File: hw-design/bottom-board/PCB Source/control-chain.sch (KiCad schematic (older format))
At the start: 20 parts, among them J15 RJHSE-5381, Q5 BSS84, Q6 BSS84, U18 ISL83086E

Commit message: change CC connector
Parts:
- removed C67, C68: 10uF, Capacitor_SMD:C_0603_1608Metric, symbol bottom-board-rescue:C_Small-Device
- removed J15: RJHSE-5381, Connector_RJ:RJ45_Amphenol_RJHSE538X, symbol bottom-board-rescue:RJ45_LED_Shielded-Connector
- removed Q5, Q6: BSS84, Package_TO_SOT_SMD:SOT-23, symbol bottom-board-rescue:BSS84-Transistor_FET
- removed R41, R42: 220R, Resistor_SMD:R_0603_1608Metric, symbol bottom-board-rescue:R_Small-Device
- added J?: RJ45, digikey-footprints:Ethernet_Jack_54602-908LF, symbol Connector:RJ45
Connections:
- net labels removed: RS485_RX_LED, RS485_TX_LED
- wire segments 87 -> 60

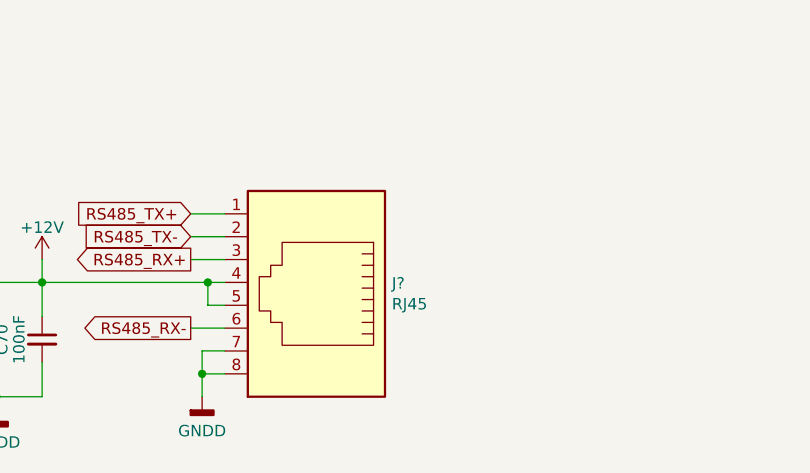
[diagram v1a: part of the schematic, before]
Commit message: place new power curcuit on the PCB
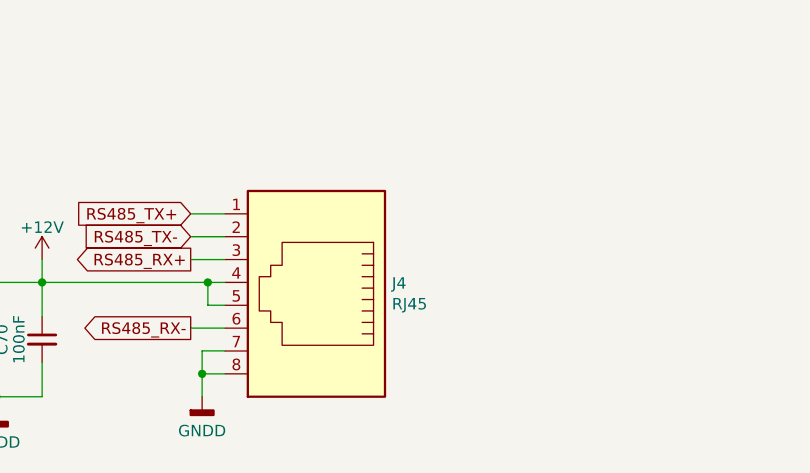
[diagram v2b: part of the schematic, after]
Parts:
- J4: renamed from J?; MPN (none) -> 54602-908LF
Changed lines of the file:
@@
 	5600 2950 5800 2950
 $Comp
-L Connector:RJ45 J?
+L Connector:RJ45 J4
 U 1 1 631709FF
 P 6150 5100
-F 0 "J?" H 5820 5104 50  0000 R CNN
+F 0 "J4" H 5820 5104 50  0000 R CNN
 F 1 "RJ45" H 5820 5195 50  0000 R CNN
 F 2 "digikey-footprints:Ethernet_Jack_54602-908LF" V 6150 5125 50  0001 C CNN
 F 3 "" V 6150 5125 50  0001 C CNN
+F 4 "54602-908LF" H 6150 5100 50  0001 C CNN "MPN"
 	1    6150 5100
 	-1   0    0    1

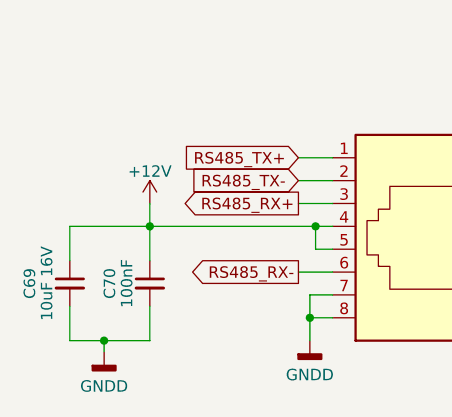
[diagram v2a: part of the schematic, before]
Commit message: update all MPN's to match the Dwarf
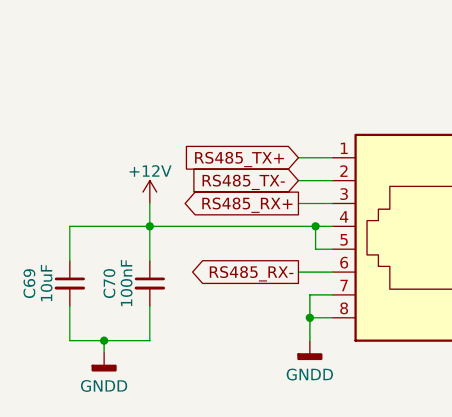
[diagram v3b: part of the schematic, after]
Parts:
- C69: value 10uF 16V -> 10uF; MPN CL21A106KOFNNNE -> GRM219R61E106KA12D
- R43, R44, R45, R46: MPN RMCF0603JT56R0 -> CRGCQ0603F56R
- R47: MPN RR0816P-101-D -> RT0603DRD07100RL
- U18: MPN ISL83086EIBZ -> ISL83491IBZ
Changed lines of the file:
@@
 Sheet 10 13
 Title "MOD DuoX - Bottom Board"
-Date "2020-05-15"
-Rev "Rev 1.12"
+Date "2021-11-11"
+Rev "Rev 1.05"
 Comp "MOD Devices GmbH"
 Comment1 "DuoX Audio processing board"
 Comment2 "https://github.com/moddevices/mod-hw-duoX"
-Comment3 ""
-Comment4 ""
+Comment3 "Inp Power: 12V 700mA"
+Comment4 "USB outp Power: 500mA"
 $EndDescr
 $Comp
@@
 F 2 "Resistor_SMD:R_0603_1608Metric" H 7550 2450 60  0001 C CNN
 F 3 "" H 7550 2450 60  0000 C CNN
-F 4 "RR0816P-101-D" H 1000 150 50  0001 C CNN "MPN"
+F 4 "RT0603DRD07100RL" H 1000 150 50  0001 C CNN "MPN"
 	1    7550 2450
 	1    0    0    -1
@@
 F 2 "Resistor_SMD:R_0603_1608Metric" H 7000 2350 60  0001 C CNN
 F 3 "" H 7000 2350 60  0000 C CNN
-F 4 "RMCF0603JT56R0" H 1000 150 50  0001 C CNN "MPN"
+F 4 "CRGCQ0603F56R" H 1000 150 50  0001 C CNN "MPN"
 	1    7000 2350
 	0    1    1    0
@@
 F 2 "Package_SO:SOIC-14_3.9x8.7mm_P1.27mm" H 6300 2750 50  0001 C CIN
 F 3 "https://www.intersil.com/content/dam/Intersil/documents/isl8/isl83080e-82e-83e-84e-85e-86e-88e.pdf" H 6300 2750 60  0001 C CNN
-F 4 "ISL83086EIBZ" H 1000 150 50  0001 C CNN "MPN"
+F 4 "ISL83491IBZ" H 1000 150 50  0001 C CNN "MPN"
 	1    6300 2750
 	1    0    0    -1
@@
 AR Path="/54F72FB6/5B818B27" Ref="C69"  Part="1"
 F 0 "C69" V 4425 5350 50  0000 C CNN
-F 1 "10uF 16V" V 4500 5350 50  0000 C CNN
+F 1 "10uF" V 4500 5350 50  0000 C CNN
 F 2 "Capacitor_SMD:C_0805_2012Metric" H 4600 5350 60  0001 C CNN
 F 3 "" H 4600 5350 60  0000 C CNN
-F 4 "CL21A106KOFNNNE" H -700 0   50  0001 C CNN "MPN"
+F 4 "GRM219R61E106KA12D" H -700 0   50  0001 C CNN "MPN"
 	1    4600 5350
 	1    0    0    -1
@@
 F 2 "Resistor_SMD:R_0603_1608Metric" H 7000 2550 60  0001 C CNN
 F 3 "" H 7000 2550 60  0000 C CNN
-F 4 "RMCF0603JT56R0" H 1000 350 50  0001 C CNN "MPN"
+F 4 "CRGCQ0603F56R" H 1000 350 50  0001 C CNN "MPN"
 	1    7000 2550
 	0    1    -1   0
@@
 F 2 "Resistor_SMD:R_0603_1608Metric" H 7250 2850 60  0001 C CNN
 F 3 "" H 7250 2850 60  0000 C CNN
-F 4 "RMCF0603JT56R0" H 1250 650 50  0001 C CNN "MPN"
+F 4 "CRGCQ0603F56R" H 1250 650 50  0001 C CNN "MPN"
 	1    7250 2850
 	0    1    1    0
@@
 F 2 "Resistor_SMD:R_0603_1608Metric" H 7250 3050 60  0001 C CNN
 F 3 "" H 7250 3050 60  0000 C CNN
-F 4 "RMCF0603JT56R0" H 1250 850 50  0001 C CNN "MPN"
+F 4 "CRGCQ0603F56R" H 1250 850 50  0001 C CNN "MPN"
 	1    7250 3050
 	0    1    -1   0
